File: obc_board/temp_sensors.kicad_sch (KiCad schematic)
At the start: 34 parts, among them U1 ADG1607, U4 LTC4304CMSTRPBF, U5 MCP9600-E_MX, U6 LT3483ES6

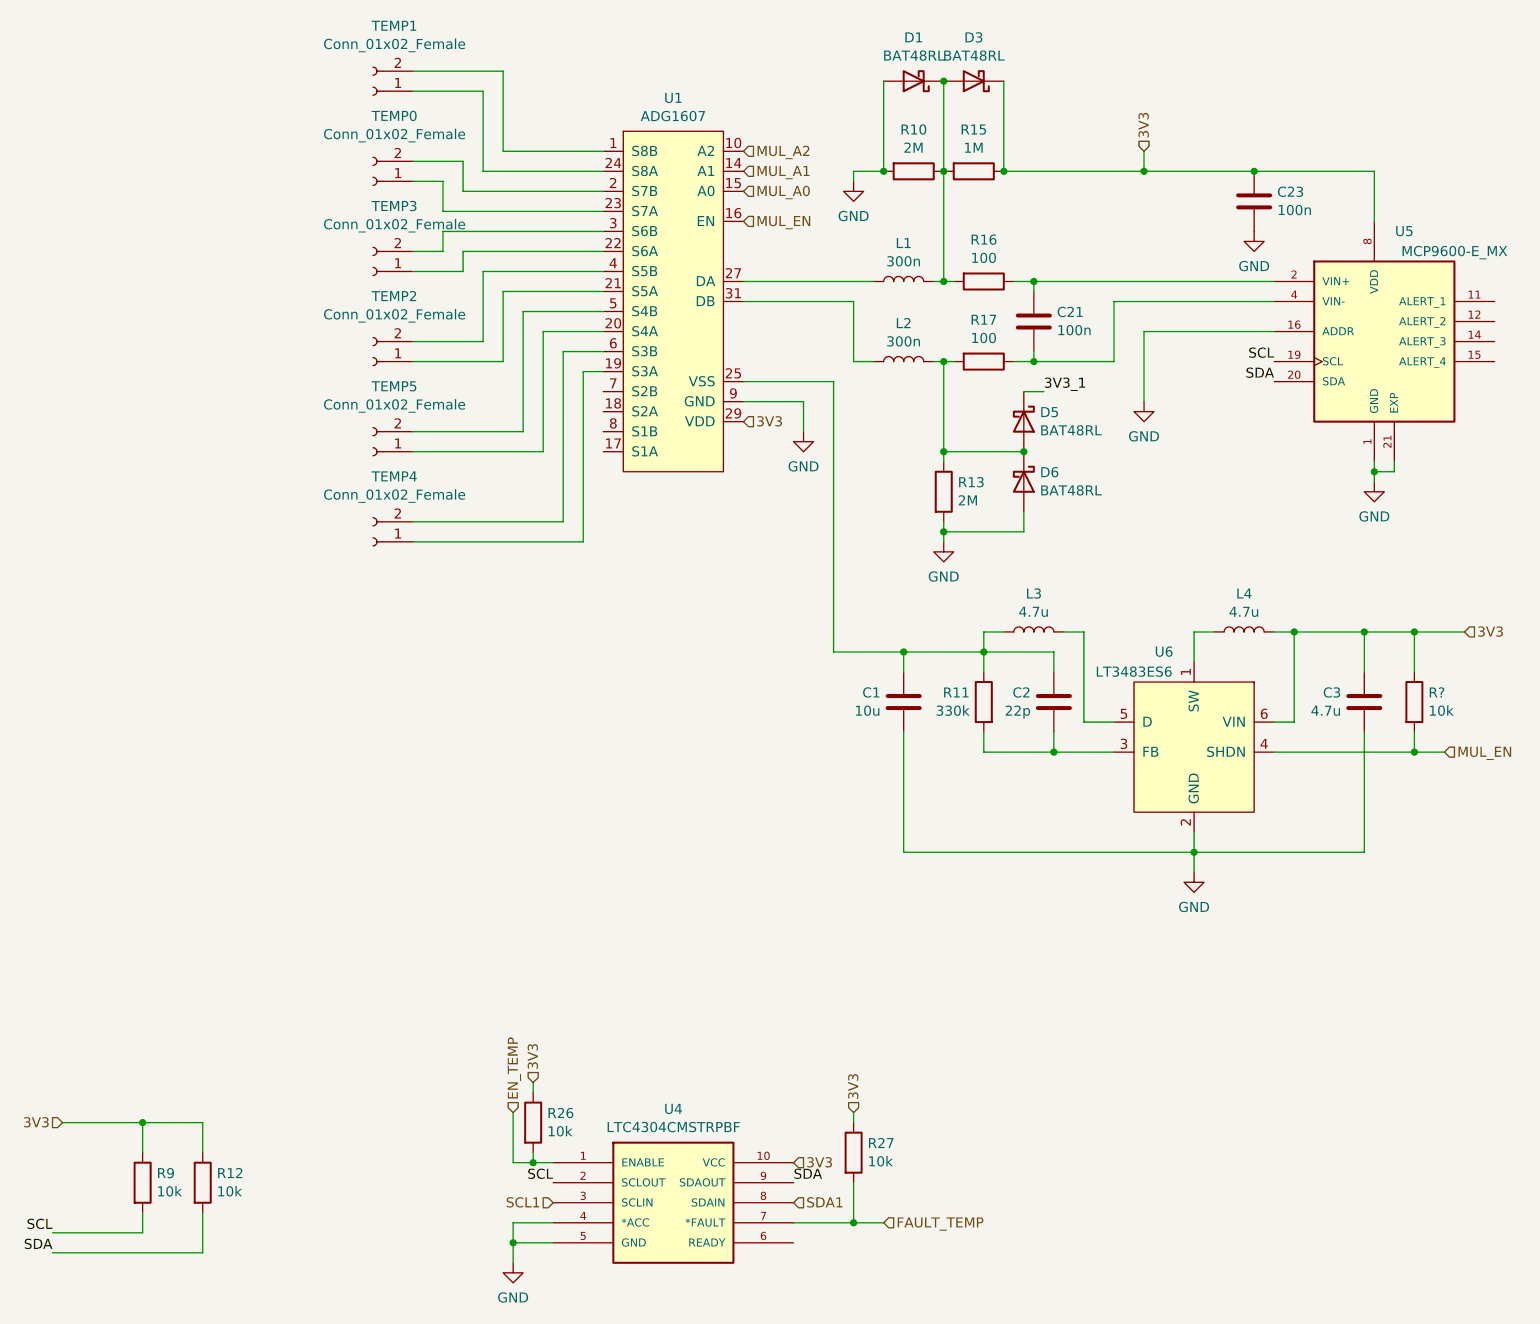
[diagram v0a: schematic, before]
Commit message: changed magnetorquer driver IC and changed power switch IC
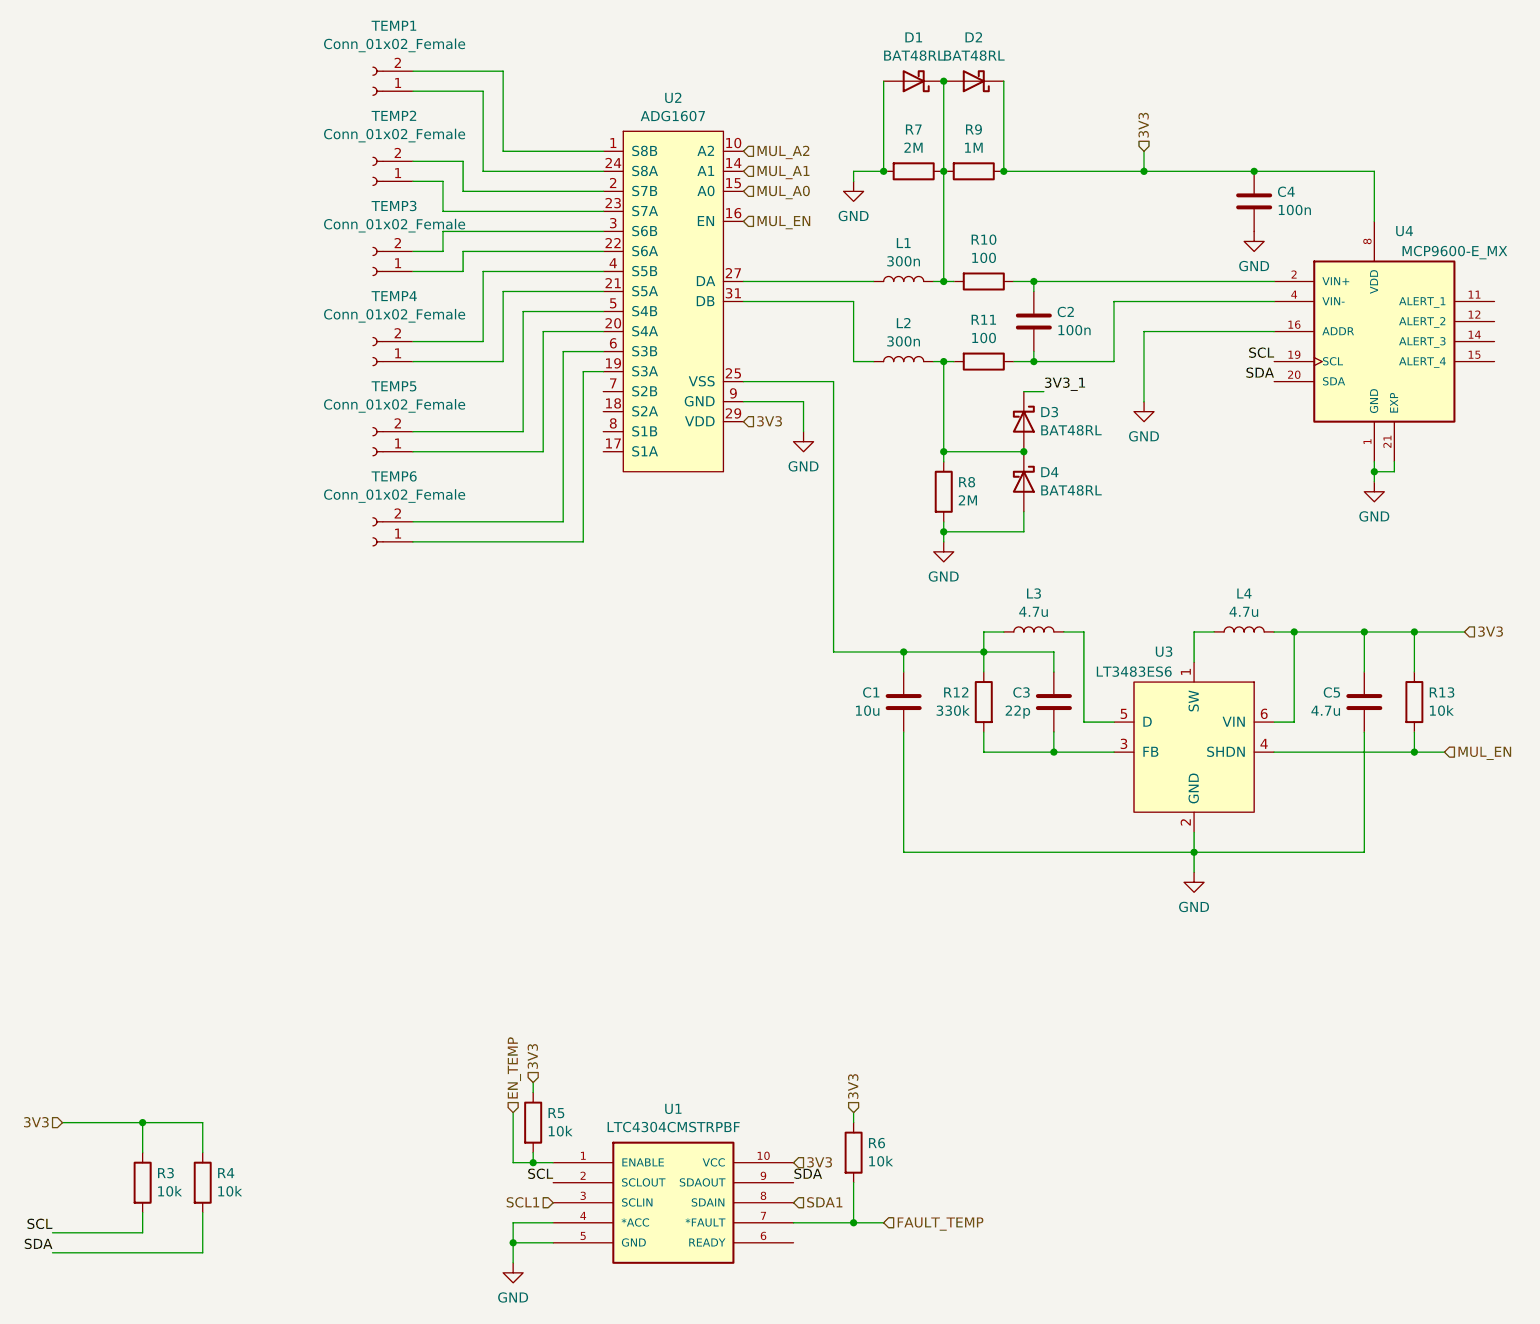
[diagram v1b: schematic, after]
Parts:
- gave numbers to parts that had none: 1
- renumbered C21 to C2, C2 to C3, C23 to C4, C3 to C5, D3 to D2, D5 to D3, D6 to D4, R16 to R10, R17 to R11, R11 to R12, R9 to R3, R12 to R4, R26 to R5, R27 to R6, R10 to R7, R13 to R8, R15 to R9, TEMP0 to TEMP2, TEMP2 to TEMP4, TEMP4 to TEMP6, U4 to U1, U1 to U2, U6 to U3, U5 to U4

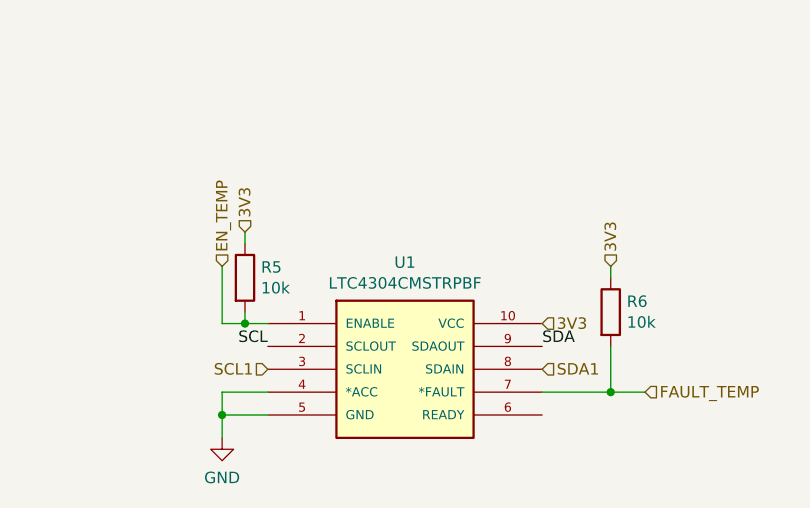
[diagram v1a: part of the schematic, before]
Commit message: updated digikey part numbers and footprints
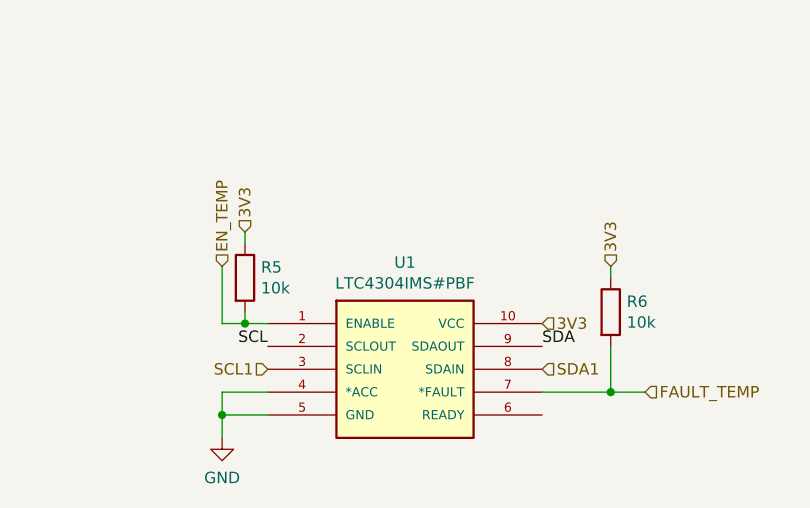
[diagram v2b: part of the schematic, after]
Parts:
- C1: Digikey Part Number 311-1952-1-ND -> 399-7012-1-ND
- C2, C4: Digikey Part Number 490-16433-1-ND -> 399-6828-1-ND
- C3: Digikey Part Number 311-1018-1-ND -> 399-C0402C220J3GACAUTOCT-ND
- C5: Digikey Part Number 490-9618-1-ND -> 399-15711-1-ND
- D1, D2, D3, D4: footprint Diode_THT:D_DO-35_SOD27_P7.62mm_Horizontal -> Diode_SMD:D_SOD-123; Digikey Part Number 497-3274-1-ND -> 497-5712-1-ND
- L1, L2: footprint Inductor_SMD:L_1210_3225Metric -> Inductor_SMD:L_Taiyo-Yuden_MD-3030; Digikey Part Number 732-7338-2-ND -> 587-5612-1-ND
- R10, R11: Digikey Part Number 311-100LRCT-ND -> YAG3435CT-ND
- R12: Digikey Part Number 311-330KLRCT-ND -> YAG3475CT-ND
- R13, R3, R4, R5, R6: Digikey Part Number 311-10.0KLRCT-ND -> YAG3436CT-ND
- R7, R8: Digikey Part Number 311-2.00MHRCT-ND -> YAG3591CT-ND
- R9: Digikey Part Number 311-1.00MHRCT-ND -> 311-1MLDCT-ND
- TEMP1, TEMP2, TEMP3, TEMP4, TEMP5, TEMP6: Digikey Part Number WM7620CT-ND -> WM25389CT-ND
- U1: value LTC4304CMSTRPBF -> LTC4304IMS#PBF; Digikey Part Number LTC4304CMS#PBF-ND -> LTC4304IMS#PBF-ND
- U4: Digikey Part Number MCP9600-E/MX-ND -> (none)

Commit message: updated pcb
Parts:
- U1: footprint MSOP-10_MS -> Package_SO:MSOP-10_3x3mm_P0.5mm
- U4: footprint QFN65P500X500X100-21N_MCP9600-E/MX -> Package_DFN_QFN:QFN-20-1EP_5x5mm_P0.65mm_EP3.35x3.35mm_ThermalVias
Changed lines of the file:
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@@
     (property "Reference" "U4" (id 0) (at 207.01 60.96 0))
     (property "Value" "MCP9600-E_MX" (id 1) (at 213.36 63.5 0))
-    (property "Footprint" "QFN65P500X500X100-21N_MCP9600-E/MX" (id 2) (at 200.66 73.66 0)
+    (property "Footprint" "Package_DFN_QFN:QFN-20-1EP_5x5mm_P0.65mm_EP3.35x3.35mm_ThermalVias" (id 2) (at 200.66 73.66 0)
       (effects (font (size 1.27 1.27)) (justify left bottom) hide)
     )
@@
     (property "Reference" "U1" (id 0) (at 114.3 172.2882 0))
     (property "Value" "LTC4304IMS#PBF" (id 1) (at 114.3 174.5996 0))
-    (property "Footprint" "MSOP-10_MS" (id 2) (at 99.06 179.07 0)
-      (effects (font (size 1.27 1.27)) (justify left bottom) hide)
-    )
+    (property "Footprint" "Package_SO:MSOP-10_3x3mm_P0.5mm" (id 2) (at 99.06 179.07 0)
+      (effects (font (size 1.27 1.27)) (justify left bottom) hide)
+    )

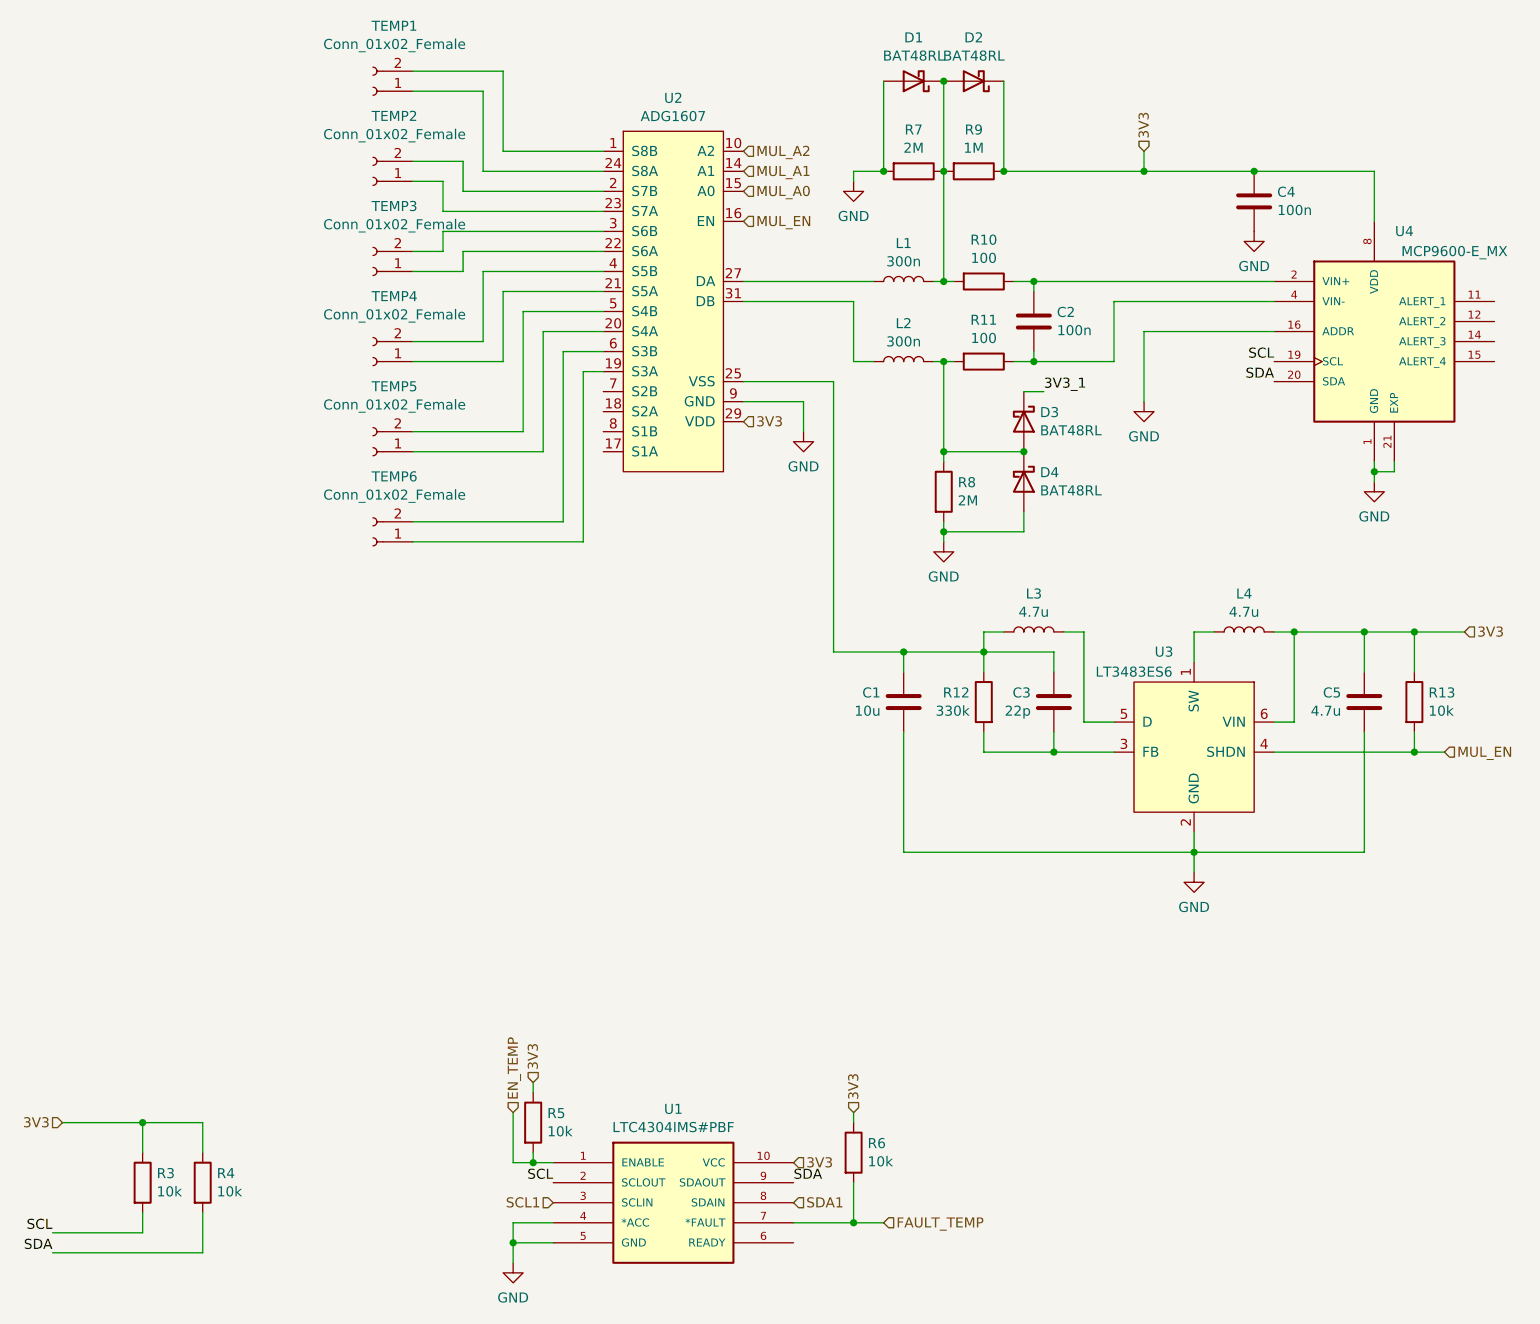
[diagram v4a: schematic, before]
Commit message: added silkscreen labels and gerber file
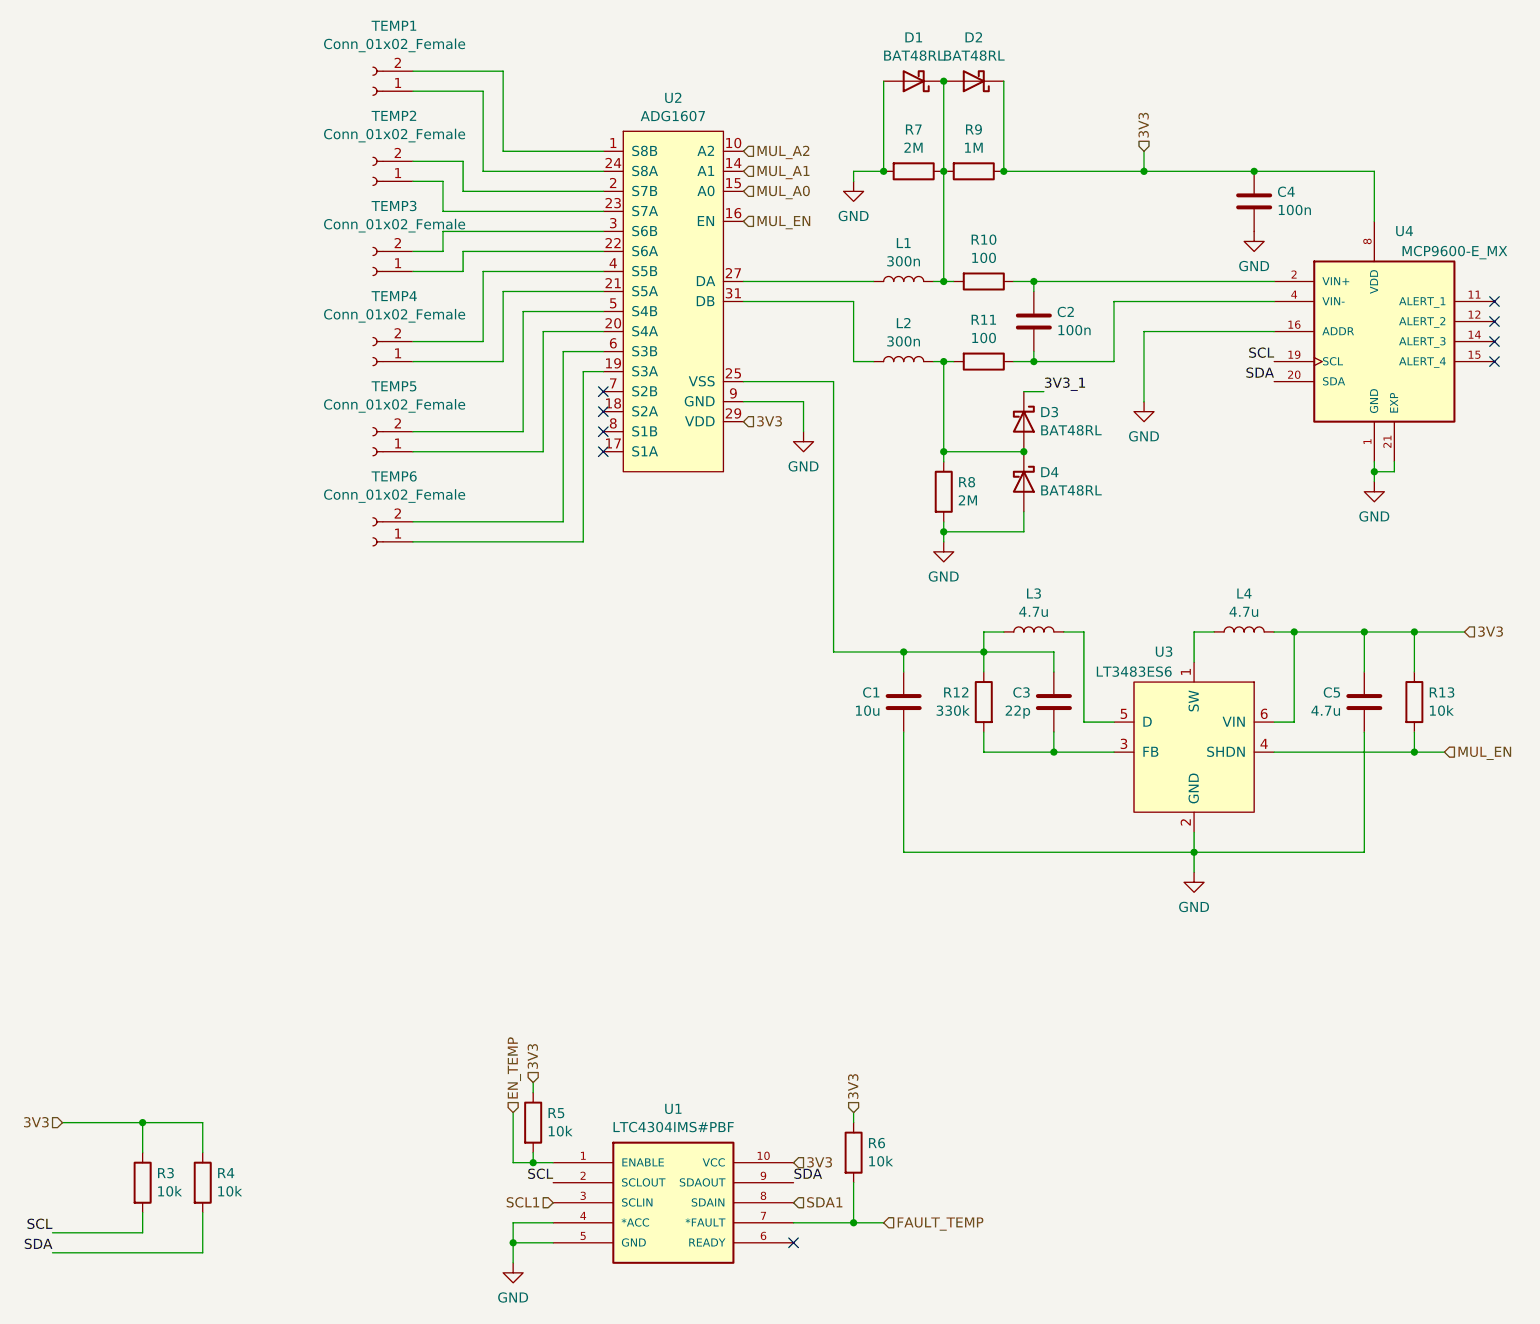
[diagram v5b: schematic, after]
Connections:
- no-connect marks 0 -> 9
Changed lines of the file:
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@@
   (junction (at 160.02 67.31) (diameter 0) (color 0 0 0 0)
   )
+  (no_connect (at 105.41 81.28))
+  (no_connect (at 105.41 86.36))
+  (no_connect (at 105.41 88.9))
+  (no_connect (at 105.41 83.82))
+  (no_connect (at 218.44 77.47))
+  (no_connect (at 218.44 74.93))
+  (no_connect (at 218.44 72.39))
+  (no_connect (at 218.44 69.85))
+  (no_connect (at 129.54 189.23))
   (wire (pts (xy 93.98 186.69) (xy 93.98 189.23))
     (stroke (width 0) (type default) (color 0 0 0 0))
